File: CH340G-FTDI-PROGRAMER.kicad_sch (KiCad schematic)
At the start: 12 parts

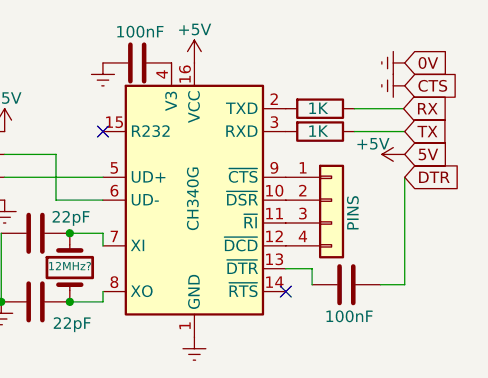
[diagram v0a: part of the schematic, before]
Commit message: CH340G FTDI Programmer V2.0
The board is ready to order, but I can`t order it rigth now, so I will have to wait about 2 months to finish this project permanently.

So the last version had the D+ and D- reversed, IDK how I did that, and more than that, I inversed the TX and RX pins and not realy. Iconnected the atmega tx to an conexion named rx, expecting ro connect RX to that pin, and same with rx. The same I done with the FTDI, and by doing that, I double reversed the tx and rx wires, so it`s like I didn`t reversed them at all.
In all that tests I saw that the 100nF capacitor at the DTR is not necesarry, and it could be just a wire in it`s place, and more than that, could be added some design changes... round corners, holes for a case, tx and rx yellow led`s, and stuff like this.
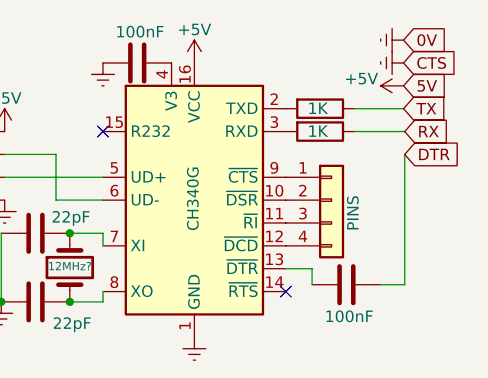
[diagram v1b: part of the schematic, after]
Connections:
- net RX: now also R?.1; no longer R?.1
- net TX: now also R?.1; no longer R?.1
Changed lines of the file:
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@@
     (stroke (width 0) (type default) (color 0 0 0 0))
   )
-  (wire (pts (xy 168.275 114.554) (xy 168.275 102.616))
+  (wire (pts (xy 168.275 114.554) (xy 168.275 100.076))
     (stroke (width 0) (type default) (color 0 0 0 0))
   )
@@
     (stroke (width 0) (type default) (color 0 0 0 0))
   )
-  (global_label "0V" (shape input) (at 168.275 89.916 0) (fields_autoplaced)
-    (effects (font (size 1.27 1.27)) (justify left))
-    (property "Intersheet References" "${INTERSHEET_REFS}" (id 0) (at 172.9862 89.8366 0)
-      (effects (font (size 1.27 1.27)) (justify left) hide)
-    )
-  )
-  (global_label "CTS" (shape input) (at 168.275 92.456 0) (fields_autoplaced)
-    (effects (font (size 1.27 1.27)) (justify left))
-    (property "Intersheet References" "${INTERSHEET_REFS}" (id 0) (at 174.1352 92.3766 0)
-      (effects (font (size 1.27 1.27)) (justify left) hide)
-    )
-  )
-  (global_label "TX" (shape input) (at 168.275 97.536 0) (fields_autoplaced)
-    (effects (font (size 1.27 1.27)) (justify left))
-    (property "Intersheet References" "${INTERSHEET_REFS}" (id 0) (at 172.8652 97.4566 0)
-      (effects (font (size 1.27 1.27)) (justify left) hide)
-    )
-  )
-  (global_label "RX" (shape input) (at 168.148 94.996 0) (fields_autoplaced)
-    (effects (font (size 1.27 1.27)) (justify left))
-    (property "Intersheet References" "${INTERSHEET_REFS}" (id 0) (at 173.0406 94.9166 0)
-      (effects (font (size 1.27 1.27)) (justify left) hide)
-    )
-  )
-  (global_label "DTR" (shape input) (at 168.275 102.616 0) (fields_autoplaced)
-    (effects (font (size 1.27 1.27)) (justify left))
-    (property "Intersheet References" "${INTERSHEET_REFS}" (id 0) (at 174.1957 102.5366 0)
-      (effects (font (size 1.27 1.27)) (justify left) hide)
-    )
-  )
-  (global_label "5V" (shape input) (at 168.275 100.076 0) (fields_autoplaced)
-    (effects (font (size 1.27 1.27)) (justify left))
-    (property "Intersheet References" "${INTERSHEET_REFS}" (id 0) (at 172.9862 99.9966 0)
+  (global_label "TX" (shape input) (at 168.148 94.996 0) (fields_autoplaced)
+    (effects (font (size 1.27 1.27)) (justify left))
+    (property "Intersheet References" "${INTERSHEET_REFS}" (id 0) (at 172.7382 94.9166 0)
+      (effects (font (size 1.27 1.27)) (justify left) hide)
+    )
+  )
+  (global_label "CTS" (shape input) (at 168.148 89.916 0) (fields_autoplaced)
+    (effects (font (size 1.27 1.27)) (justify left))
+    (property "Intersheet References" "${INTERSHEET_REFS}" (id 0) (at 174.0082 89.8366 0)
+      (effects (font (size 1.27 1.27)) (justify left) hide)
+    )
+  )
+  (global_label "RX" (shape input) (at 168.275 97.536 0) (fields_autoplaced)
+    (effects (font (size 1.27 1.27)) (justify left))
+    (property "Intersheet References" "${INTERSHEET_REFS}" (id 0) (at 173.1676 97.4566 0)
+      (effects (font (size 1.27 1.27)) (justify left) hide)
+    )
+  )
+  (global_label "5V" (shape input) (at 168.148 92.456 0) (fields_autoplaced)
+    (effects (font (size 1.27 1.27)) (justify left))
+    (property "Intersheet References" "${INTERSHEET_REFS}" (id 0) (at 172.8592 92.3766 0)
+      (effects (font (size 1.27 1.27)) (justify left) hide)
+    )
+  )
+  (global_label "0V" (shape input) (at 168.148 87.376 0) (fields_autoplaced)
+    (effects (font (size 1.27 1.27)) (justify left))
+    (property "Intersheet References" "${INTERSHEET_REFS}" (id 0) (at 172.8592 87.2966 0)
+      (effects (font (size 1.27 1.27)) (justify left) hide)
+    )
+  )
+  (global_label "DTR" (shape input) (at 168.275 100.076 0) (fields_autoplaced)
+    (effects (font (size 1.27 1.27)) (justify left))
+    (property "Intersheet References" "${INTERSHEET_REFS}" (id 0) (at 174.1957 99.9966 0)
       (effects (font (size 1.27 1.27)) (justify left) hide)
     )
@@
     (pin "4")
   )
-  (symbol (lib_id "power:Earth") (at 168.275 89.916 270) (mirror x) (unit 1)
-    (in_bom yes) (on_board yes) (fields_autoplaced)
-    (property "Reference" "#PWR?" (id 0) (at 161.925 89.916 0)
-      (effects (font (size 1.27 1.27)) hide)
-    )
-    (property "Value" "Earth" (id 1) (at 164.465 89.916 0)
-      (effects (font (size 1.27 1.27)) hide)
-    )
-    (property "Footprint" "" (id 2) (at 168.275 89.916 0)
-      (effects (font (size 1.27 1.27)) hide)
-    )
-    (property "Datasheet" "~" (id 3) (at 168.275 89.916 0)
-      (effects (font (size 1.27 1.27)) hide)
-    )
-    (pin "1")
-  )
-  (symbol (lib_id "power:Earth") (at 168.275 92.456 270) (mirror x) (unit 1)
-    (in_bom yes) (on_board yes) (fields_autoplaced)
-    (property "Reference" "#PWR?" (id 0) (at 161.925 92.456 0)
-      (effects (font (size 1.27 1.27)) hide)
-    )
-    (property "Value" "Earth" (id 1) (at 164.465 92.456 0)
-      (effects (font (size 1.27 1.27)) hide)
-    )
-    (property "Footprint" "" (id 2) (at 168.275 92.456 0)
-      (effects (font (size 1.27 1.27)) hide)
-    )
-    (property "Datasheet" "~" (id 3) (at 168.275 92.456 0)
-      (effects (font (size 1.27 1.27)) hide)
-    )
-    (pin "1")
-  )
   (symbol (lib_id "power:Earth") (at 134.747 89.916 0) (mirror y) (unit 1)
     (in_bom yes) (on_board yes) (fields_autoplaced)
@@
     (pin "1")
     (pin "2")
+  )
+  (symbol (lib_id "power:+5V") (at 168.148 92.456 90) (mirror x) (unit 1)
+    (in_bom yes) (on_board yes)
+    (property "Reference" "#PWR?" (id 0) (at 171.958 92.456 0)
+      (effects (font (size 1.27 1.27)) hide)
+    )
+    (property "Value" "+5V" (id 1) (at 163.449 91.694 90))
+    (property "Footprint" "" (id 2) (at 168.148 92.456 0)
+      (effects (font (size 1.27 1.27)) hide)
+    )
+    (property "Datasheet" "" (id 3) (at 168.148 92.456 0)
+      (effects (font (size 1.27 1.27)) hide)
+    )
+    (pin "1")
   )
   (symbol (lib_id "Device:C") (at 138.557 89.916 270) (mirror x) (unit 1)
@@
     (pin "2")
   )
-  (symbol (lib_id "power:+5V") (at 168.275 100.076 90) (mirror x) (unit 1)
-    (in_bom yes) (on_board yes)
-    (property "Reference" "#PWR?" (id 0) (at 172.085 100.076 0)
-      (effects (font (size 1.27 1.27)) hide)
-    )
-    (property "Value" "+5V" (id 1) (at 164.719 98.933 90))
-    (property "Footprint" "" (id 2) (at 168.275 100.076 0)
-      (effects (font (size 1.27 1.27)) hide)
-    )
-    (property "Datasheet" "" (id 3) (at 168.275 100.076 0)
+  (symbol (lib_id "power:Earth") (at 168.148 89.916 270) (mirror x) (unit 1)
+    (in_bom yes) (on_board yes) (fields_autoplaced)
+    (property "Reference" "#PWR?" (id 0) (at 161.798 89.916 0)
+      (effects (font (size 1.27 1.27)) hide)
+    )
+    (property "Value" "Earth" (id 1) (at 164.338 89.916 0)
+      (effects (font (size 1.27 1.27)) hide)
+    )
+    (property "Footprint" "" (id 2) (at 168.148 89.916 0)
+      (effects (font (size 1.27 1.27)) hide)
+    )
+    (property "Datasheet" "~" (id 3) (at 168.148 89.916 0)
       (effects (font (size 1.27 1.27)) hide)
     )
@@
     (pin "1")
   )
+  (symbol (lib_id "power:Earth") (at 168.148 87.376 270) (mirror x) (unit 1)
+    (in_bom yes) (on_board yes) (fields_autoplaced)
+    (property "Reference" "#PWR?" (id 0) (at 161.798 87.376 0)
+      (effects (font (size 1.27 1.27)) hide)
+    )
+    (property "Value" "Earth" (id 1) (at 164.338 87.376 0)
+      (effects (font (size 1.27 1.27)) hide)
+    )
+    (property "Footprint" "" (id 2) (at 168.148 87.376 0)
+      (effects (font (size 1.27 1.27)) hide)
+    )
+    (property "Datasheet" "~" (id 3) (at 168.148 87.376 0)
+      (effects (font (size 1.27 1.27)) hide)
+    )
+    (pin "1")
+  )
   (symbol (lib_id "Device:C") (at 127.254 116.459 90) (mirror x) (unit 1)
     (in_bom yes) (on_board yes)
@@
       (reference "#PWR?") (unit 1) (value "Earth") (footprint "")
     )
-    (path "/47223ffc-c6f6-4ac8-8a2c-e468799379e7"
-      (reference "#PWR?") (unit 1) (value "Earth") (footprint "")
-    )
-    (path "/4a977ab9-4f2e-499a-bd44-c75104b50751"
-      (reference "#PWR?") (unit 1) (value "Earth") (footprint "")
-    )
     (path "/4e552225-2ec9-4aad-8e9e-7006e5acc30a"
       (reference "#PWR?") (unit 1) (value "Earth") (footprint "")
+    )
+    (path "/57b03263-2554-4315-bda7-ecfc44ce2028"
+      (reference "#PWR?") (unit 1) (value "+5V") (footprint "")
     )
     (path "/73064269-f293-491f-9139-186cb72528f3"
@@
       (reference "#PWR?") (unit 1) (value "Earth") (footprint "")
     )
-    (path "/9c92a24b-c9b3-4dba-98aa-6bb60dd71ed7"
-      (reference "#PWR?") (unit 1) (value "+5V") (footprint "")
+    (path "/a43dfc45-04de-4760-86a8-e6811f18f6fe"
+      (reference "#PWR?") (unit 1) (value "Earth") (footprint "")
     )
     (path "/a92d9107-32d0-4528-9d5f-96f5f4c922c7"
@@
       (reference "#PWR?") (unit 1) (value "Earth") (footprint "")
     )
+    (path "/c75aa7d8-bb17-42a9-ace9-aa7500f1d547"
+      (reference "#PWR?") (unit 1) (value "Earth") (footprint "")
+    )

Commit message: V2
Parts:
- X1: renamed from 12MHz?; value Crystal -> 12MHz
- gave numbers to parts that had none: 9

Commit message: qq
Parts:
- removed C1, C2: 100nF, symbol Device:C
- removed C3: 22pF, symbol Device:C
- removed J1: PINS, symbol Connector_Generic_MountingPin:Conn_01x04_MountingPin
- removed J?: USB, symbol Connector:USB_A
- removed U?: CH340G, Package_SO:SOIC-16_3.9x9.9mm_P1.27mm, symbol Interface_USB:CH340G
- removed X1: 12MHz, symbol Device:Crystal
- added C1, C2: 100uF, Capacitor_SMD:C_1210_3225Metric_Pad1.33x2.70mm_HandSolder, symbol Device:C_Polarized_US
- added C10, C6, C9: 100nF, symbol Device:C
- added C7, C8: 22pF, symbol Device:C
- added D2: BLUE, symbol Device:LED
- added J1, J2: USB, symbol Connector:USB_A
- added J2, J3: PINS, symbol Connector_Generic_MountingPin:Conn_01x04_MountingPin
- added J3: Conn_01x03_Pin, symbol Connector:Conn_01x03_Pin
- added J4: Conn_01x06_Pin, symbol Connector:Conn_01x06_Pin
- added R4, R5, R6: 1K, symbol Device:R
- added U2 (x2): CH340G, Package_SO:SOIC-16_3.9x9.9mm_P1.27mm, symbol Interface_USB:CH340G
- added U2: AMS1117-3.3, Package_TO_SOT_SMD:SOT-223-3_TabPin2, symbol Regulator_Linear:AMS1117-3.3
- added X2: 12MHz, symbol Device:Crystal
- added Y1: 12MHz, Crystal:Resonator_SMD_Murata_CSTxExxV-3Pin_3.0x1.1mm, symbol Device:Resonator
- C4: value 22pF -> 100nF
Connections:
- net +5V: now also C1.1, D2.1 (K), J1.1 (VCC), J2.1 (VCC), J3.3 (Pin_3), U2.16 (VCC), U2.3 (VI); no longer D1.1 (K)
- net DTR: now also C10.1
- net Earth: now also C4.2, R1.1, C1.2, C2.2, C7.1, C8.1, C9.2, J1.4 (GND), J2.4 (GND), J4.5 (Pin_5), J4.6 (Pin_6), R4.1, U2.1 (GND), U2.1 (GND), U2.1 (GND), Y1.2; no longer C4.1, R3.1
- net RX: now also R6.1; no longer R2.1
- net TX: now also R5.1; no longer R1.1
- net at R1.2: now also D1.2 (A)
- net at R2.2: now also U2.2 (TXD)
- net at R3.2: now also U2.3 (RXD); no longer D1.2 (A)
- new net: J3.2 (Pin_2), U2.10 (~{DSR})
- new net: J3.3 (Pin_3), U2.11 (~{RI})
- new net: J3.4 (Pin_4), U2.12 (~{DCD})
- new net: C10.2, U2.13 (~{DTR})
- new net: R5.2, U2.2 (TXD)
- new net: R6.2, U2.3 (RXD)
- new net: C9.1, U2.4 (V3)
- new net: J2.3 (D+), U2.5 (UD+)
- new net: J2.2 (D-), U2.6 (UD-)
- new net: C7.2, U2.7 (XI), X2.1
- new net: C8.2, U2.8 (XO), X2.2
- new net: J3.1 (Pin_1), U2.9 (~{CTS})
- new net: D2.2 (A), R4.2
- new net: C6.1, J4.1 (Pin_1)
- new net: C6.2, U2.13 (~{DTR})
- new net: J1.2 (D-), U2.6 (UD-)
- new net: J1.3 (D+), U2.5 (UD+)
- new net: J2.1 (Pin_1), U2.12 (~{DCD})
- new net: J2.2 (Pin_2), U2.11 (~{RI})
- new net: J2.3 (Pin_3), U2.10 (~{DSR})
- new net: J2.4 (Pin_4), U2.9 (~{CTS})
- new net: J4.2 (Pin_2), R3.1
- new net: C4.1, U2.4 (V3)
- new net: U2.7 (XI), Y1.1
- new net: U2.8 (XO), Y1.3
- new net: J4.3 (Pin_3), R2.1
- new net +3.3V: C2.1, J3.1 (Pin_1), U2.2 (VO)
- new net VCC: D1.1 (K), J3.2 (Pin_2), J4.4 (Pin_4), U2.16 (VCC)
- no-connect marks 2 -> 4
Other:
- note added: "V2.0"
- note added: "V2.1"
